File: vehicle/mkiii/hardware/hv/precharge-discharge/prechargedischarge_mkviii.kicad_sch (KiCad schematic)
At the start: 65 parts, among them J2 Conn_01x03_Pin, J3 CONN_pcie_x1, J4 Conn_01x03_Pin, K1 G2RG-2A-X_DC12, K2 3350-4275-126, K3 G2RG-2A-X_DC12, Q1 SSM3K333R, Q2 SSM3K333R, U1 ACNT-H61L-500E, U2 LM397, U3 MP9488, U6 74LVC2G00, U7 74LVC2G08

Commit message: precharge discharge: replace kicad files from old repo
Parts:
- removed R27, R29: 100 kΩ, Resistor_SMD:R_1206_3216Metric, symbol Device:R
- removed U1: ACNT-H61L-500E, Package_SO:SOIC-8_7.5x5.85mm_P1.27mm, symbol Isolator:6N136
- removed U6: 74LVC2G00, Package_SO:SOIC-8_3.9x4.9mm_P1.27mm, symbol 74xGxx:74LVC2G00
- removed U7: 74LVC2G08, Package_SO:SOIC-8_3.9x4.9mm_P1.27mm, symbol 74xGxx:74LVC2G08
- added C11: C_1uF_25V, OEM:C_0603_1608Metric, symbol OEM:C_1uF_25V_0603
- added C12, C13: C_0.1uF, OEM:C_0603_1608Metric, symbol OEM:C_0.1uF
- added C14: 0.1 µF, Capacitor_SMD:C_0603_1608Metric, symbol Device:C
- added D11: 1N4148W, Diode_SMD:D_SOD-123, symbol Diode:1N4148W
- added D12: BSPD_TRIP_LED, OEM:D_0805_2012Metric, symbol OEM:LED_RED
- added R30: R_1K, OEM:R_0603_1608Metric, symbol OEM:R_1K
- added R31: R_100k, OEM:R_0603_1608Metric, symbol OEM:R_100k_0.1W_0603
- added R32: R_10K, OEM:R_0603_1608Metric, symbol OEM:R_10K
- added R35: 100 kΩ, OEM:R_0603_1608Metric, symbol Device:R
- added R36: R_10k, OEM:R_0603_1608Metric, symbol OEM:R_10k_0.1W_0603
- added U1, U6: U_GATE_SN74LVC1G02DBVR, OEM:SOT-23-5, symbol OEM:U_GATE_SN74LVC1G02DBVR
- added U4: ACNT-H50L-500E, OEM:ACNT-H50L-500E, symbol OEM:ACNT-H50L-500E
- added U5: 74LVC1GU04DRL, Package_TO_SOT_SMD:SOT-553, symbol 74xGxx:74LVC1GU04DRL
- added U7, U8: SN74LVC1G08DBVR, OEM:SOT-23-5, symbol OEM:U_AND-Gate_SN74LVC1G08DBVR_SOT23-5new
- C9: footprint Capacitor_THT:CP_Radial_D8.0mm_P3.50mm -> Capacitor_THT:CP_Radial_D10.0mm_P5.00mm
- D8: footprint Diode_SMD:D_SMA -> OEM:D_SOD-128
- F1: footprint OEM:Fuse_1206_3216Metric -> footprints:F_21mA_420V
- F2: footprint OEM:Fuse_1206_3216Metric -> footprints:Fuse_1210
- L1: footprint Inductor_SMD:L_Wuerth_HCM-1390 -> footprints:L_1.2mH
- R10: footprint OEM:R_0603 -> OEM:R_0603_1608Metric
- R26: footprint Resistor_SMD:R_1206_3216Metric -> OEM:R_0603_1608Metric
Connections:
- net +5V: now also C12.1, C13.1, C14.1, R36.2, U1.5 (VCC), U4.8, U5.5 (VCC), U6.5 (VCC), U7.5 (VCC), U8.5 (VCC)
- net DONE_ISO: now also R36.1, U4.6, U5.2
- net DONE_LATCHED: now also U1.1 (in), U6.4 (out), U7.1
- net DONE_LATCHED_N: now also R30.1, R32.1, U1.4 (out), U6.2 (in), U8.1
- net GND: now also C11.2, C12.2, C13.2, C14.2, D12.1 (K), R32.2, R35.1, U1.3 (GND), U4.5, U5.3 (GND), U6.3 (GND), U7.3 (GND), U8.3 (GND)
- net PRECHARGE_DONE_N: now also U4.3
- net PRECHARGE_LSD: now also R35.2, U1.2 (in), U7.2, U8.2
- net PRECHARGE_LSD_1: now also U8.4
- net PRECHARGE_LSD_2: now also D11.2 (A), R31.2, U7.4; no longer Q2.1 (G), R12.1
- net at R26.2: now also U4.2
- new net: D12.2 (A), R30.2
- new net: C11.1, D11.1 (K), Q2.1 (G), R12.1, R31.1
- new net DONE_ISO_N: U5.4, U6.1 (in)
- no-connect marks 31 -> 33
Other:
- note added: "Replace with Nor Latch - SR (Nand)"
- moved on the sheet: C5, C6, Q2, R12, R26

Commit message: precharge discharge: fixed rc delay math and fixed diode facing wrong direction
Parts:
- C11: value C_1uF_25V -> C_2.2uF_25V
- R12: value 10KR -> 1MR
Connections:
- net PRECHARGE_LSD_2: now also D11.1 (K); no longer D11.2 (A)
- net at C11.1, Q2.1 (G), R12.1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: now also D11.2 (A); no longer D11.1 (K)
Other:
- moved on the sheet: D11
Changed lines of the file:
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@@
 		(at 256.54 82.55)
 	)
-	(bus_entry
-		(at 77.47 73.66)
-		(size 2.54 2.54)
-		(stroke
-			(width 0)
-			(type default)
-		)
-	)
-	(bus_entry
-		(at 60.96 59.69)
-		(size 2.54 2.54)
-		(stroke
-			(width 0)
-			(type default)
-		)
-	)
 	(wire
 		(pts
@@
 			)
 		)
-		(property "Value" "C_1uF_25V"
+		(property "Value" "C_2.2uF_25V"
 			(at 182.88 119.3799 0)
 			(effects
@@
 	(symbol
 		(lib_id "Diode:1N4148W")
-		(at 172.72 110.49 180)
+		(at 172.72 110.49 0)
 		(unit 1)
 		(exclude_from_sim no)
@@
 		)
 		(property "Footprint" "Diode_SMD:D_SOD-123"
-			(at 172.72 106.045 0)
+			(at 172.72 114.935 0)
 			(effects
 				(font
@@
 			)
 		)
-		(property "Value" "10KR"
+		(property "Value" "1MR"
 			(at 176.53 109.2201 0)
 			(effects

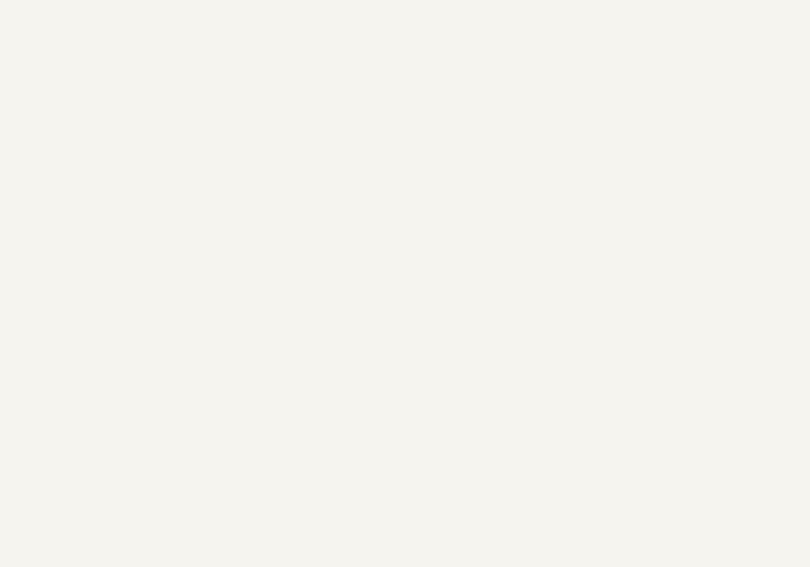
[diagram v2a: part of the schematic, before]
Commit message: precharge-discarge: Added final changes(Made left side of board smaller, added mounting holes, added lv led, 2mm between planes, disconnect nc pins
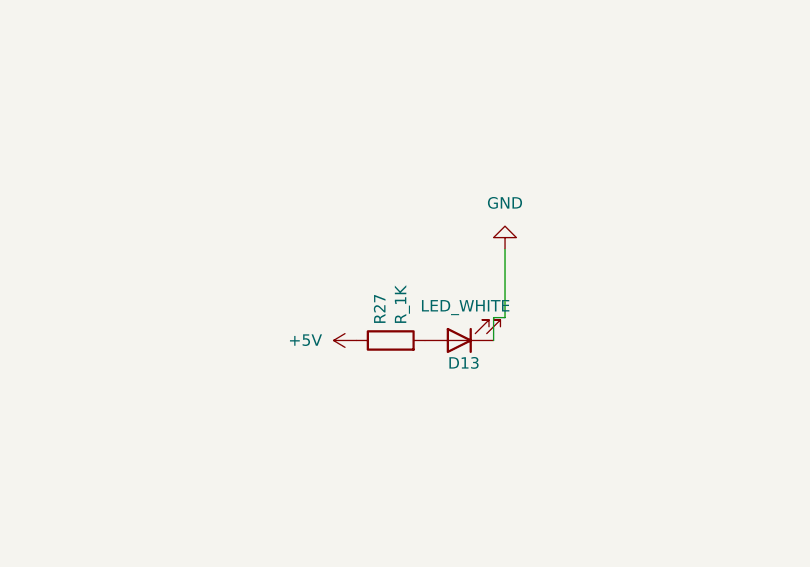
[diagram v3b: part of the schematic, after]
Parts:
- added D13: LED_WHITE, LED_SMD:LED_0805_2012Metric, symbol OEM:LED_WHITE
- added R27: R_1K, OEM:R_0603_1608Metric, symbol OEM:1KR
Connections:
- net +5V: now also R27.1
- net GND: now also D13.1 (K)
- new net: D13.2 (A), R27.2

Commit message: MkVIII precharge/discharge: Fiona's advice implemented better via routing and better wiring
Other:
- note removed: "F1 and F2 MP9488 Sumida RCP1317 optocoupler latch"
- note removed: "Symbols that need footprint update:"
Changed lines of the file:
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@@
-		)
-	)
-	(text "F1 and F2\nMP9488\nSumida RCP1317\noptocoupler\nlatch"
-		(exclude_from_sim no)
-		(at 39.624 276.606 0)
-		(effects
-			(font
-				(size 1.27 1.27)
-			)
 		)
 	)
@@
 		(effects
 			(font
-				(size 1.27 1.27)
-			)
-		)
-	)
-	(text "Symbols that need footprint update:"
-		(exclude_from_sim no)
-		(at 40.132 268.732 0)
-		(effects
-			(font

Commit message: Precharge-Discharge: Rerouted vias, changed optocoupler values based on documentation and added resitors to comparator in order to prevent threshold fluctuation
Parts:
- added R29: R_4.7M, OEM:R_0603_1608Metric, symbol OEM:R_10K
- added R33: R_10k, OEM:R_0603_1608Metric, symbol OEM:R_10K
- R12: value 1MR -> 270kR
- R26: value 1 kΩ -> 330Ω
- R31: value R_100k -> R_71.5k
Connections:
- net +5V_TS_FUSED: now also R33.2
- net PRECHARGE_DONE_N: now also R29.1, R33.1
- net V_DC_SENSE: now also R29.2
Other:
- note added: "all zones on one side 2mm form each other solid pads for zones make wires on relay be more far apart"
- moved on the sheet: D11, J3

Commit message: Precharge Discharge: Fixed non latching SR Latch Logic and minor board tweaks
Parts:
- added C15, C16: 0.1 µF, Capacitor_SMD:C_0603_1608Metric, symbol Device:C
- added C17: C_10nF, OEM:C_0603_1608Metric, symbol OEM:C_0.1uF
- added R34: 100 kΩ, OEM:R_0603_1608Metric, symbol Device:R
- added U10: SN74LVC1G08DBVR, OEM:SOT-23-5, symbol OEM:U_AND-Gate_SN74LVC1G08DBVR_SOT23-5new
- added U9: 74LVC1GU04DRL, Package_TO_SOT_SMD:SOT-553, symbol 74xGxx:74LVC1GU04DRL
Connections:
- net +5V: now also C15.1, C16.1, U10.5 (VCC), U9.5 (VCC)
- net DONE_ISO_N: now also U10.1; no longer U6.1 (in)
- net GND: now also C15.2, C16.2, C17.1, R34.1, U10.3 (GND), U9.3 (GND)
- net PRECHARGE_LSD: now also C17.2, R34.2, U10.2, U9.2; no longer R35.2, U1.2 (in)
- new net DONE_ISO_SET: R35.2, U1.2 (in), U10.4
- new net PRECHARGE_LSD_N: U6.1 (in), U9.4
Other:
- note added: "Only populate if signal is noisy (capacitor C17)"
- note removed: "all zones on one side 2mm form each other solid pads for zones make wires on relay be more far apart"
